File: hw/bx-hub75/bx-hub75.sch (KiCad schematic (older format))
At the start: 1 part

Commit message: hw/bx-hub75: hook up HUB75 to line drivers.
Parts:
- removed FPGA?: Bx, FPGAs:TinyFPGA_BX, symbol FPGAs:Bx
- added CHAIN1: HUB75_HEADER, symbol Random:HUB75_HEADER
- added FPGA1: Bx, symbol TinyFPGA:Bx
- added U1, U2: 74HCT244, symbol 74xx:74HCT244
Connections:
- net labels added: +5V, A, B, B1, B2, C, CLK, D, G1, G2, GND, LAT, OE, R1, R2
- wire segments 0 -> 51

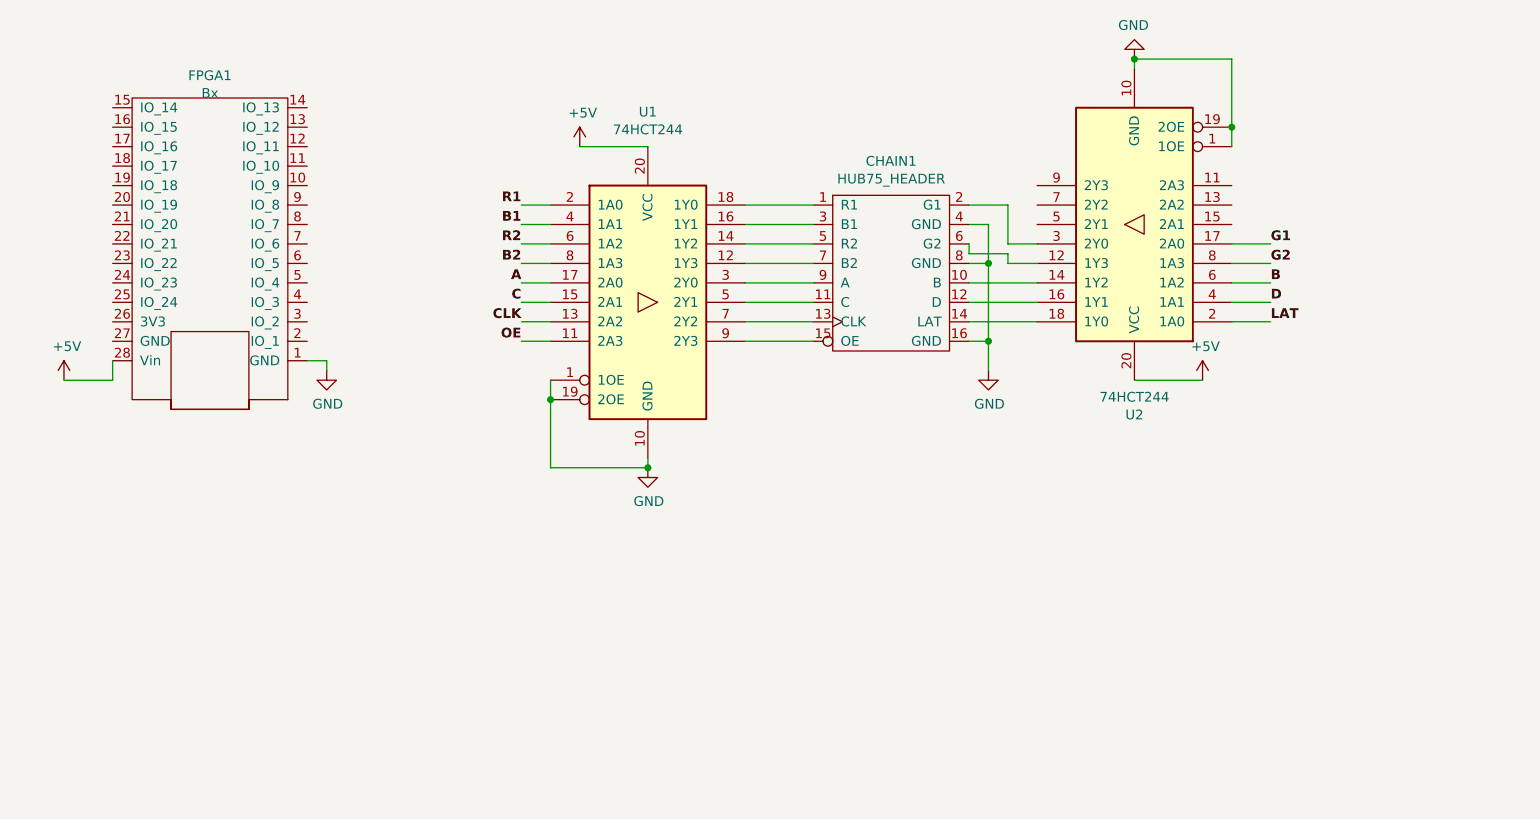
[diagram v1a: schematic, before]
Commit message: hw/bx-hub75: hook up RS485 and line drivers to FPGA.
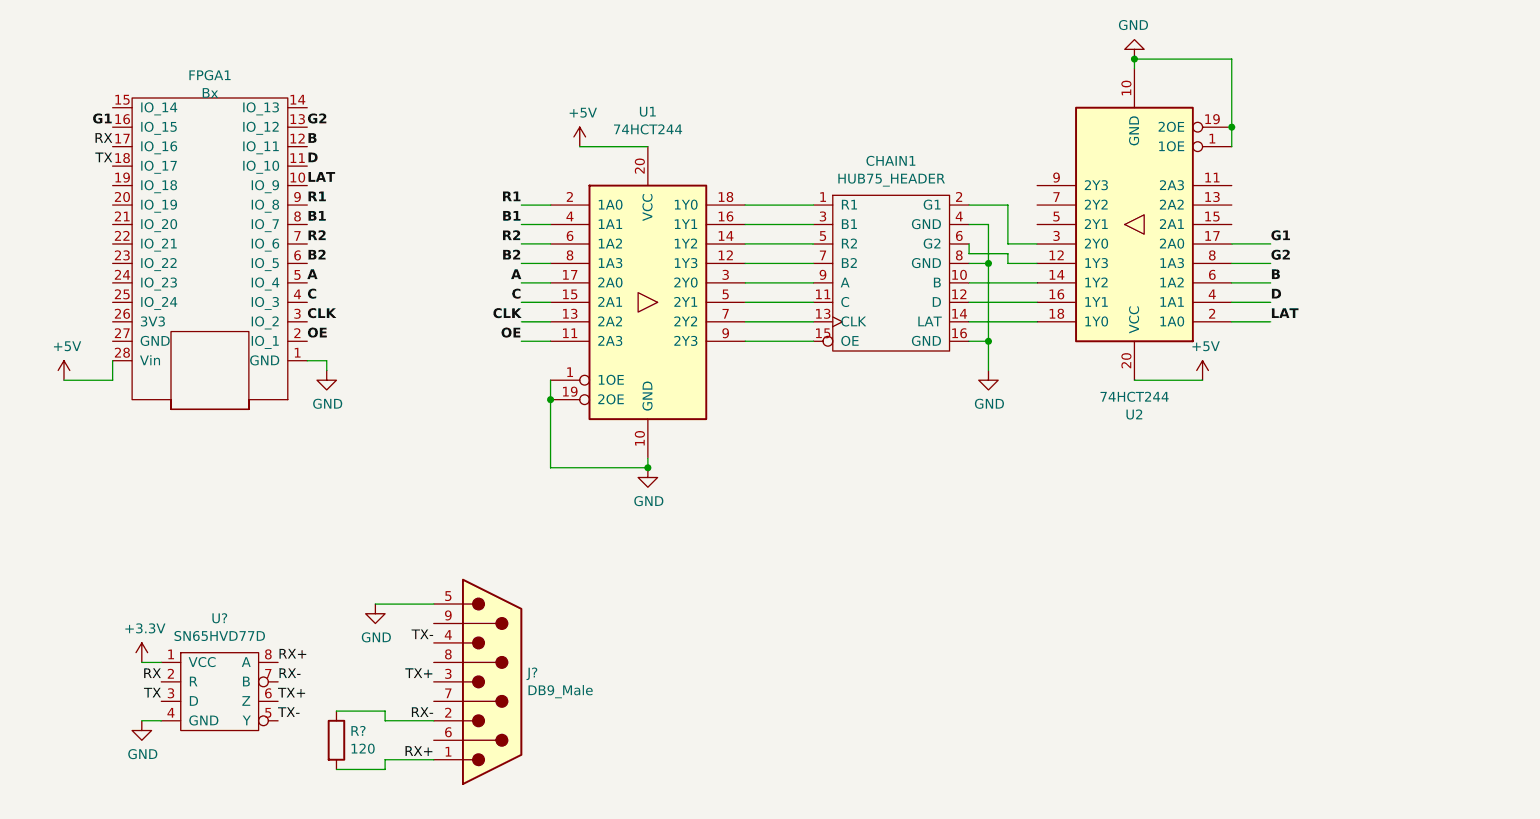
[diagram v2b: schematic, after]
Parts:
- added J?: DB9_Male, symbol Connector:DB9_Male
- added R?: 120, symbol Device:R
- added U?: SN65HVD77D, symbol Random:SN65HVD77D
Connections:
- net A: now also FPGA1.5 (IO_4)
- net B: now also FPGA1.12 (IO_11)
- net B1: now also FPGA1.8 (IO_7)
- net B2: now also FPGA1.6 (IO_5)
- net C: now also FPGA1.4 (IO_3)
- net CLK: now also FPGA1.3 (IO_2)
- net D: now also FPGA1.11 (IO_10)
- net G1: now also FPGA1.16 (IO_15)
- net G2: now also FPGA1.13 (IO_12)
- net GND: now also J?.5, U?.4 (GND)
- net LAT: now also FPGA1.10 (IO_9)
- net OE: now also FPGA1.2 (IO_1)
- net R1: now also FPGA1.9 (IO_8)
- net R2: now also FPGA1.7 (IO_6)
- net RX: now reaches FPGA1.17 (IO_16)
- net RX: now also U?.2 (R)
- net TX: now reaches FPGA1.18 (IO_17)
- net TX: now also U?.3 (D)
- new net +3V3: U?.1 (VCC)
- new net RX+: J?.1, R?.2, U?.8 (A)
- new net RX-: J?.2, R?.1, U?.7 (B)
- new net TX+: J?.3, U?.6 (Z)
- new net TX-: J?.4, U?.5 (Y)
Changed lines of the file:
@@
 	6850 3350 6850 3500
 Connection ~ 6850 3350
+Text Label 3350 3350 0    50   ~ 10
+OE
+Text Label 3350 3250 0    50   ~ 10
+CLK
+Text Label 3350 3150 0    50   ~ 10
+C
+Text Label 3350 3050 0    50   ~ 10
+A
+Text Label 3350 2950 0    50   ~ 10
+B2
+Text Label 3350 2850 0    50   ~ 10
+R2
+Text Label 3350 2750 0    50   ~ 10
+B1
+Text Label 3350 2650 0    50   ~ 10
+R1
+Text Label 3350 2550 0    50   ~ 10
+LAT
+Text Label 3350 2450 0    50   ~ 10
+D
+Text Label 3350 2350 0    50   ~ 10
+B
+Text Label 3350 2250 0    50   ~ 10
+G2
+Text Label 2350 2250 2    50   ~ 10
+G1
+$Comp
+L Random:SN65HVD77D U?
+U 1 1 5BECF5D6
+P 2900 5150
+F 0 "U?" H 2900 5525 50  0000 C CNN
+F 1 "SN65HVD77D" H 2900 5434 50  0000 C CNN
+F 2 "" H 2900 4900 50  0001 C CNN
+F 3 "" H 2900 4900 50  0001 C CNN
+	1    2900 5150
+	1    0    0    -1
+$EndComp
+$Comp
+L power:+3.3V #PWR?
+U 1 1 5BECFB36
+P 2500 5000
+F 0 "#PWR?" H 2500 4850 50  0001 C CNN
+F 1 "+3.3V" H 2515 5173 50  0000 C CNN
+F 2 "" H 2500 5000 50  0001 C CNN
+F 3 "" H 2500 5000 50  0001 C CNN
+	1    2500 5000
+	1    0    0    -1
+$EndComp
+$Comp
+L power:GND #PWR?
+U 1 1 5BECFBC2
+P 2500 5300
+F 0 "#PWR?" H 2500 5050 50  0001 C CNN
+F 1 "GND" H 2505 5127 50  0000 C CNN
+F 2 "" H 2500 5300 50  0001 C CNN
+F 3 "" H 2500 5300 50  0001 C CNN
+	1    2500 5300
+	1    0    0    -1
+$EndComp
+Wire Wire Line
+	2500 5300 2600 5300
+Wire Wire Line
+	2500 5000 2600 5000
+Text Label 2600 5100 2    50   ~ 0
+RX
+Text Label 2600 5200 2    50   ~ 0
+TX
+$Comp
+L Connector:DB9_Male J?
+U 1 1 5BED180D
+P 4300 5100
+F 0 "J?" H 4480 5146 50  0000 L CNN
+F 1 "DB9_Male" H 4480 5055 50  0000 L CNN
+F 2 "" H 4300 5100 50  0001 C CNN
+F 3 " ~" H 4300 5100 50  0001 C CNN
+	1    4300 5100
+	1    0    0    -1
+$EndComp
+Text Label 3200 5000 0    50   ~ 0
+RX+
+Text Label 3200 5100 0    50   ~ 0
+RX-
+Text Label 3200 5200 0    50   ~ 0
+TX+
+Text Label 3200 5300 0    50   ~ 0
+TX-
+Text Label 4000 5500 2    50   ~ 0
+RX+
+Text Label 4000 5300 2    50   ~ 0
+RX-
+Text Label 4000 5100 2    50   ~ 0
+TX+
+Text Label 4000 4900 2    50   ~ 0
+TX-
+$Comp
+L power:GND #PWR?
+U 1 1 5BEDE34B
+P 3700 4700
+F 0 "#PWR?" H 3700 4450 50  0001 C CNN
+F 1 "GND" H 3705 4527 50  0000 C CNN
+F 2 "" H 3700 4700 50  0001 C CNN
+F 3 "" H 3700 4700 50  0001 C CNN
+	1    3700 4700
+	1    0    0    -1
+$EndComp
+Wire Wire Line
+	3700 4700 4000 4700
+$Comp
+L Device:R R?
+U 1 1 5BEE0AE3
+P 3500 5400
+F 0 "R?" H 3570 5446 50  0000 L CNN
+F 1 "120" H 3570 5355 50  0000 L CNN
+F 2 "" V 3430 5400 50  0001 C CNN
+F 3 "~" H 3500 5400 50  0001 C CNN
+	1    3500 5400
+	1    0    0    -1
+$EndComp
+Wire Wire Line
+	4000 5300 3750 5300
+Wire Wire Line
+	3750 5300 3750 5250
+Wire Wire Line
+	3750 5250 3500 5250
+Wire Wire Line
+	3500 5550 3750 5550
+Wire Wire Line
+	3750 5550 3750 5500
+Wire Wire Line
+	3750 5500 4000 5500
+Text Label 2350 2350 2    50   ~ 0
+RX
+Text Label 2350 2450 2    50   ~ 0
+TX
 $EndSCHEMATC

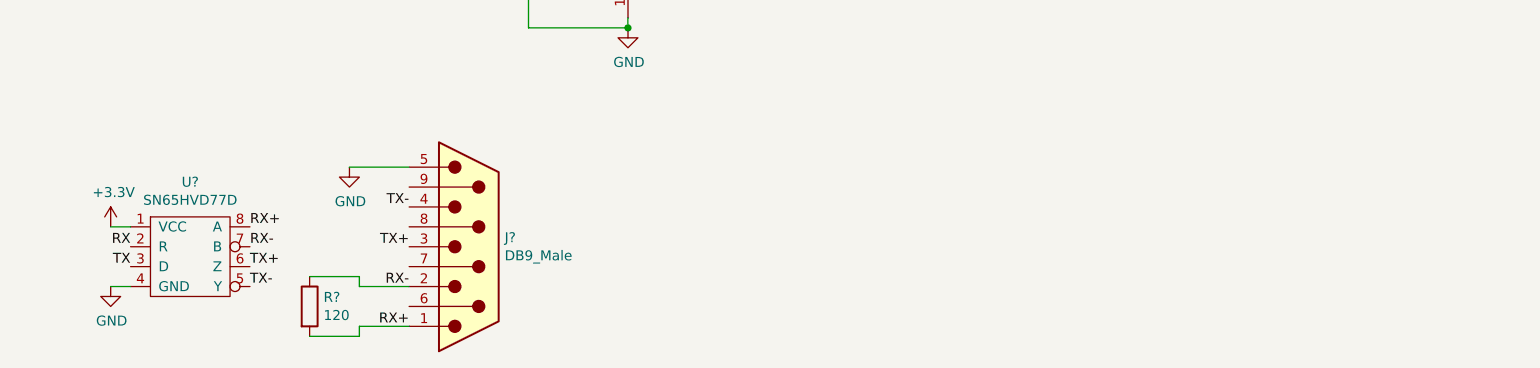
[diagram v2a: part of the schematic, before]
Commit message: hw/bx-hub75: 3.3V VREG
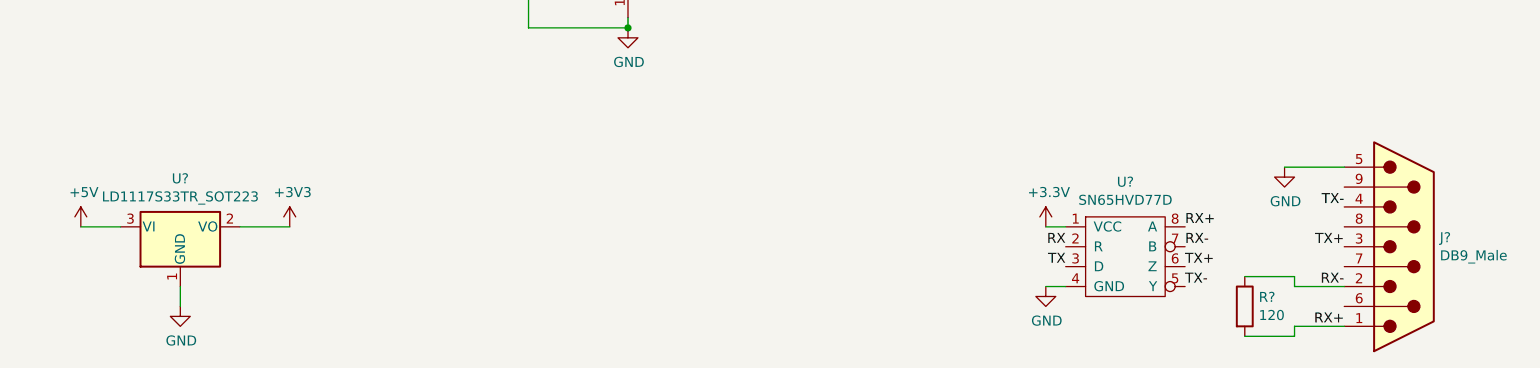
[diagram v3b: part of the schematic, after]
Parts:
- added U?: LD1117S33TR_SOT223, Package_TO_SOT_SMD:SOT-223-3_TabPin2, symbol Regulator_Linear:LD1117S33TR_SOT223
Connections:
- net +3V3: now also U?.2 (VO)
- net +5V: now also U?.3 (VI)
- net GND: now also U?.1 (GND)
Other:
- moved on the sheet: J?, R?, U?
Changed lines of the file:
@@
 L Random:SN65HVD77D U?
 U 1 1 5BECF5D6
-P 2900 5150
-F 0 "U?" H 2900 5525 50  0000 C CNN
-F 1 "SN65HVD77D" H 2900 5434 50  0000 C CNN
-F 2 "" H 2900 4900 50  0001 C CNN
-F 3 "" H 2900 4900 50  0001 C CNN
-	1    2900 5150
+P 7600 5150
+F 0 "U?" H 7600 5525 50  0000 C CNN
+F 1 "SN65HVD77D" H 7600 5434 50  0000 C CNN
+F 2 "" H 7600 4900 50  0001 C CNN
+F 3 "" H 7600 4900 50  0001 C CNN
+	1    7600 5150
 	1    0    0    -1
 $EndComp
@@
 L power:+3.3V #PWR?
 U 1 1 5BECFB36
-P 2500 5000
-F 0 "#PWR?" H 2500 4850 50  0001 C CNN
-F 1 "+3.3V" H 2515 5173 50  0000 C CNN
-F 2 "" H 2500 5000 50  0001 C CNN
-F 3 "" H 2500 5000 50  0001 C CNN
-	1    2500 5000
+P 7200 5000
+F 0 "#PWR?" H 7200 4850 50  0001 C CNN
+F 1 "+3.3V" H 7215 5173 50  0000 C CNN
+F 2 "" H 7200 5000 50  0001 C CNN
+F 3 "" H 7200 5000 50  0001 C CNN
+	1    7200 5000
 	1    0    0    -1
 $EndComp
@@
 L power:GND #PWR?
 U 1 1 5BECFBC2
-P 2500 5300
-F 0 "#PWR?" H 2500 5050 50  0001 C CNN
-F 1 "GND" H 2505 5127 50  0000 C CNN
-F 2 "" H 2500 5300 50  0001 C CNN
-F 3 "" H 2500 5300 50  0001 C CNN
-	1    2500 5300
+P 7200 5300
+F 0 "#PWR?" H 7200 5050 50  0001 C CNN
+F 1 "GND" H 7205 5127 50  0000 C CNN
+F 2 "" H 7200 5300 50  0001 C CNN
+F 3 "" H 7200 5300 50  0001 C CNN
+	1    7200 5300
 	1    0    0    -1
 $EndComp
 Wire Wire Line
-	2500 5300 2600 5300
+	7200 5300 7300 5300
 Wire Wire Line
-	2500 5000 2600 5000
-Text Label 2600 5100 2    50   ~ 0
+	7200 5000 7300 5000
+Text Label 7300 5100 2    50   ~ 0
 RX
-Text Label 2600 5200 2    50   ~ 0
+Text Label 7300 5200 2    50   ~ 0
 TX
 $Comp
 L Connector:DB9_Male J?
 U 1 1 5BED180D
-P 4300 5100
-F 0 "J?" H 4480 5146 50  0000 L CNN
-F 1 "DB9_Male" H 4480 5055 50  0000 L CNN
-F 2 "" H 4300 5100 50  0001 C CNN
-F 3 " ~" H 4300 5100 50  0001 C CNN
-	1    4300 5100
+P 9000 5100
+F 0 "J?" H 9180 5146 50  0000 L CNN
+F 1 "DB9_Male" H 9180 5055 50  0000 L CNN
+F 2 "" H 9000 5100 50  0001 C CNN
+F 3 " ~" H 9000 5100 50  0001 C CNN
+	1    9000 5100
 	1    0    0    -1
 $EndComp
-Text Label 3200 5000 0    50   ~ 0
+Text Label 7900 5000 0    50   ~ 0
 RX+
-Text Label 3200 5100 0    50   ~ 0
+Text Label 7900 5100 0    50   ~ 0
 RX-
-Text Label 3200 5200 0    50   ~ 0
+Text Label 7900 5200 0    50   ~ 0
 TX+
-Text Label 3200 5300 0    50   ~ 0
+Text Label 7900 5300 0    50   ~ 0
 TX-
-Text Label 4000 5500 2    50   ~ 0
+Text Label 8700 5500 2    50   ~ 0
 RX+
-Text Label 4000 5300 2    50   ~ 0
+Text Label 8700 5300 2    50   ~ 0
 RX-
-Text Label 4000 5100 2    50   ~ 0
+Text Label 8700 5100 2    50   ~ 0
 TX+
-Text Label 4000 4900 2    50   ~ 0
+Text Label 8700 4900 2    50   ~ 0
 TX-
 $Comp
 L power:GND #PWR?
 U 1 1 5BEDE34B
-P 3700 4700
-F 0 "#PWR?" H 3700 4450 50  0001 C CNN
-F 1 "GND" H 3705 4527 50  0000 C CNN
-F 2 "" H 3700 4700 50  0001 C CNN
-F 3 "" H 3700 4700 50  0001 C CNN
-	1    3700 4700
+P 8400 4700
+F 0 "#PWR?" H 8400 4450 50  0001 C CNN
+F 1 "GND" H 8405 4527 50  0000 C CNN
+F 2 "" H 8400 4700 50  0001 C CNN
+F 3 "" H 8400 4700 50  0001 C CNN
+	1    8400 4700
 	1    0    0    -1
 $EndComp
 Wire Wire Line
-	3700 4700 4000 4700
+	8400 4700 8700 4700
 $Comp
 L Device:R R?
 U 1 1 5BEE0AE3
-P 3500 5400
-F 0 "R?" H 3570 5446 50  0000 L CNN
-F 1 "120" H 3570 5355 50  0000 L CNN
-F 2 "" V 3430 5400 50  0001 C CNN
-F 3 "~" H 3500 5400 50  0001 C CNN
-	1    3500 5400
+P 8200 5400
+F 0 "R?" H 8270 5446 50  0000 L CNN
+F 1 "120" H 8270 5355 50  0000 L CNN
+F 2 "" V 8130 5400 50  0001 C CNN
+F 3 "~" H 8200 5400 50  0001 C CNN
+	1    8200 5400
 	1    0    0    -1
 $EndComp
 Wire Wire Line
-	4000 5300 3750 5300
+	8700 5300 8450 5300
 Wire Wire Line
-	3750 5300 3750 5250
+	8450 5300 8450 5250
 Wire Wire Line
-	3750 5250 3500 5250
+	8450 5250 8200 5250
 Wire Wire Line
-	3500 5550 3750 5550
+	8200 5550 8450 5550
 Wire Wire Line
-	3750 5550 3750 5500
+	8450 5550 8450 5500
 Wire Wire Line
-	3750 5500 4000 5500
+	8450 5500 8700 5500
 Text Label 2350 2350 2    50   ~ 0
 RX
 Text Label 2350 2450 2    50   ~ 0
 TX
+$Comp
+L Regulator_Linear:LD1117S33TR_SOT223 U?
+U 1 1 5BEF264A
+P 2850 5000
+F 0 "U?" H 2850 5242 50  0000 C CNN
+F 1 "LD1117S33TR_SOT223" H 2850 5151 50  0000 C CNN
+F 2 "Package_TO_SOT_SMD:SOT-223-3_TabPin2" H 2850 5200 50  0001 C CNN
+F 3 "http://www.st.com/st-web-ui/static/active/en/resource/technical/document/datasheet/CD00000544.pdf" H 2950 4750 50  0001 C CNN
+	1    2850 5000
+	1    0    0    -1
+$EndComp
+$Comp
+L power:+5V #PWR?
+U 1 1 5BEF2B74
+P 2350 5000
+F 0 "#PWR?" H 2350 4850 50  0001 C CNN
+F 1 "+5V" H 2365 5173 50  0000 C CNN
+F 2 "" H 2350 5000 50  0001 C CNN
+F 3 "" H 2350 5000 50  0001 C CNN
+	1    2350 5000
+	1    0    0    -1
+$EndComp
+$Comp
+L power:GND #PWR?
+U 1 1 5BEF2BC3
+P 2850 5400
+F 0 "#PWR?" H 2850 5150 50  0001 C CNN
+F 1 "GND" H 2855 5227 50  0000 C CNN
+F 2 "" H 2850 5400 50  0001 C CNN
+F 3 "" H 2850 5400 50  0001 C CNN
+	1    2850 5400
+	1    0    0    -1
+$EndComp
+Wire Wire Line
+	2850 5300 2850 5400
+Wire Wire Line
+	2550 5000 2350 5000
+$Comp
+L power:+3V3 #PWR?
+U 1 1 5BEF8C03
+P 3400 5000
+F 0 "#PWR?" H 3400 4850 50  0001 C CNN
+F 1 "+3V3" H 3415 5173 50  0000 C CNN
+F 2 "" H 3400 5000 50  0001 C CNN
+F 3 "" H 3400 5000 50  0001 C CNN
+	1    3400 5000
+	1    0    0    -1
+$EndComp
+Wire Wire Line
+	3400 5000 3150 5000
 $EndSCHEMATC
